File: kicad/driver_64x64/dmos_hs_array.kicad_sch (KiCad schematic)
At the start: 18 parts

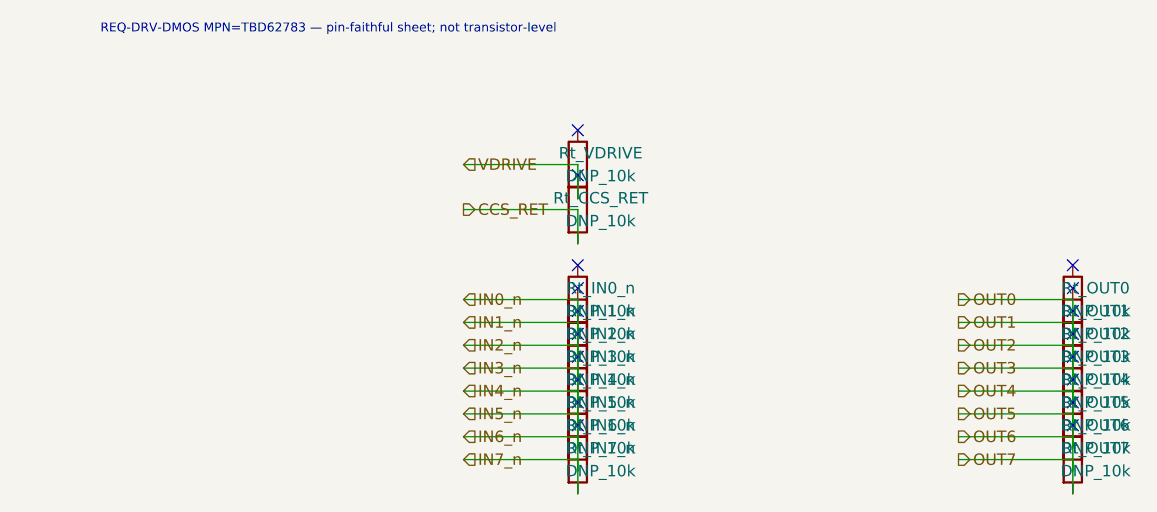
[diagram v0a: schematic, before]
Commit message: logical seperation into host and multiple decode/drive/steering boards
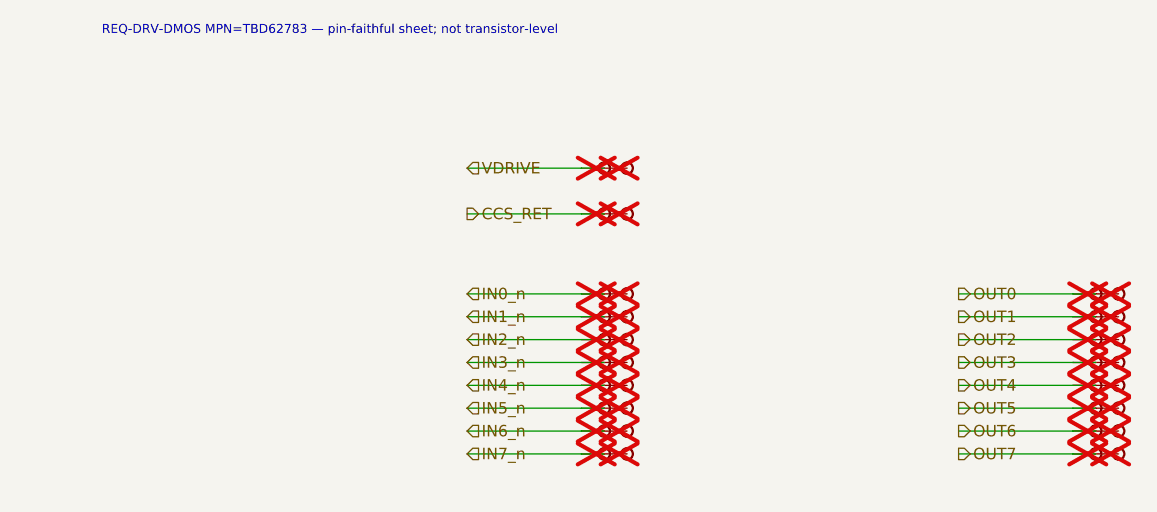
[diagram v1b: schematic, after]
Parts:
- removed Rt_CCS_RET, Rt_IN0_n, Rt_IN1_n, Rt_IN2_n, Rt_IN3_n, Rt_IN4_n, Rt_IN5_n, Rt_IN6_n, Rt_IN7_n, Rt_OUT0, Rt_OUT1, Rt_OUT2, Rt_OUT3, Rt_OUT4, Rt_OUT5, Rt_OUT6, Rt_OUT7, Rt_VDRIVE: DNP_10k, symbol Device:R
- added TP_CCS_RET, TP_CCS_RETb, TP_IN0_n, TP_IN0_nb, TP_IN1_n, TP_IN1_nb, TP_IN2_n, TP_IN2_nb, TP_IN3_n, TP_IN3_nb, TP_IN4_n, TP_IN4_nb, TP_IN5_n, TP_IN5_nb, TP_IN6_n, TP_IN6_nb, TP_IN7_n, TP_IN7_nb, TP_OUT0, TP_OUT0b, TP_OUT1, TP_OUT1b, TP_OUT2, TP_OUT2b, TP_OUT3, TP_OUT3b, TP_OUT4, TP_OUT4b, TP_OUT5, TP_OUT5b, TP_OUT6, TP_OUT6b, TP_OUT7, TP_OUT7b, TP_VDRIVE, TP_VDRIVEb: Stub, symbol CMR:Stub
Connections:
- net CCS_RET: now also TP_CCS_RET.1, TP_CCS_RETb.1
- net IN0_n: now also TP_IN0_n.1, TP_IN0_nb.1
- net OUT0: now also TP_OUT0.1, TP_OUT0b.1
- net VDRIVE: now also TP_VDRIVE.1, TP_VDRIVEb.1
- new net IN1_n: TP_IN1_n.1, TP_IN1_nb.1
- new net IN2_n: TP_IN2_n.1, TP_IN2_nb.1
- new net IN3_n: TP_IN3_n.1, TP_IN3_nb.1
- new net IN4_n: TP_IN4_n.1, TP_IN4_nb.1
- new net IN5_n: TP_IN5_n.1, TP_IN5_nb.1
- new net IN6_n: TP_IN6_n.1, TP_IN6_nb.1
- new net IN7_n: TP_IN7_n.1, TP_IN7_nb.1
- new net OUT1: TP_OUT1.1, TP_OUT1b.1
- new net OUT2: TP_OUT2.1, TP_OUT2b.1
- new net OUT3: TP_OUT3.1, TP_OUT3b.1
- new net OUT4: TP_OUT4.1, TP_OUT4b.1
- new net OUT5: TP_OUT5.1, TP_OUT5b.1
- new net OUT6: TP_OUT6.1, TP_OUT6b.1
- new net OUT7: TP_OUT7.1, TP_OUT7b.1
- no-connect marks 18 -> 0
